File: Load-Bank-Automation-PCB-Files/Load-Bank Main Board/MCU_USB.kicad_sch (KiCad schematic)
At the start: 19 parts, among them J26 STM32-Prog-Header, SW2 SW_SPDT, SW4 RESET, U13 STM32G491VETx, U2 OXETDLJANF-8MHz

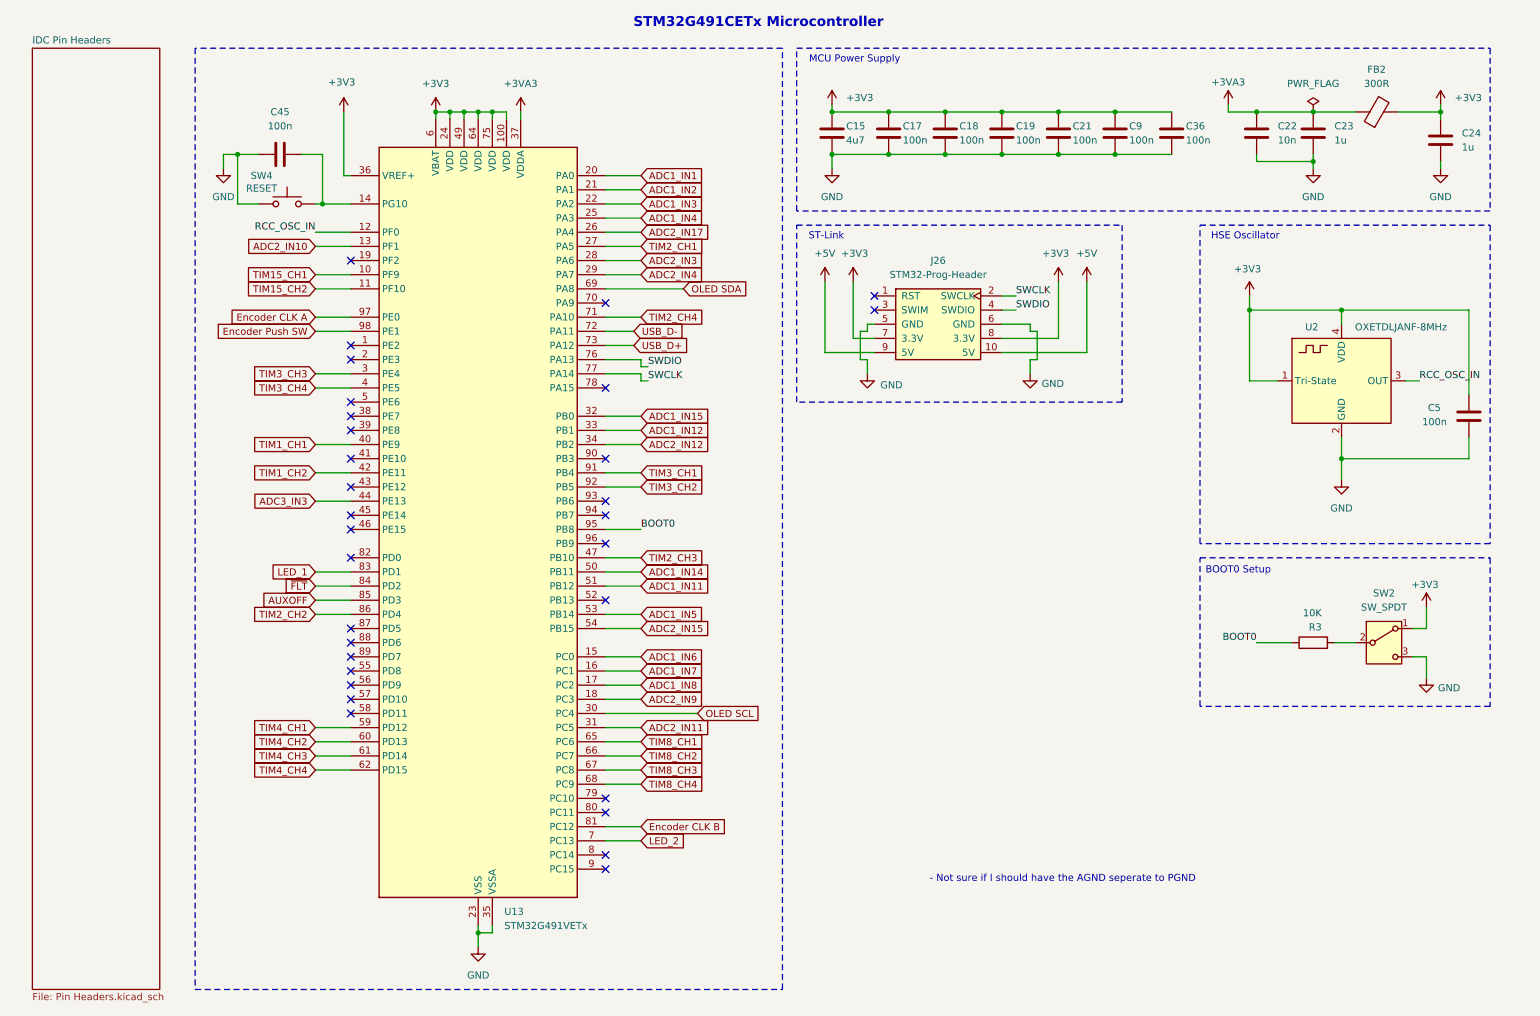
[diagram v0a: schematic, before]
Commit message: All footprints assigned and new schematic changes
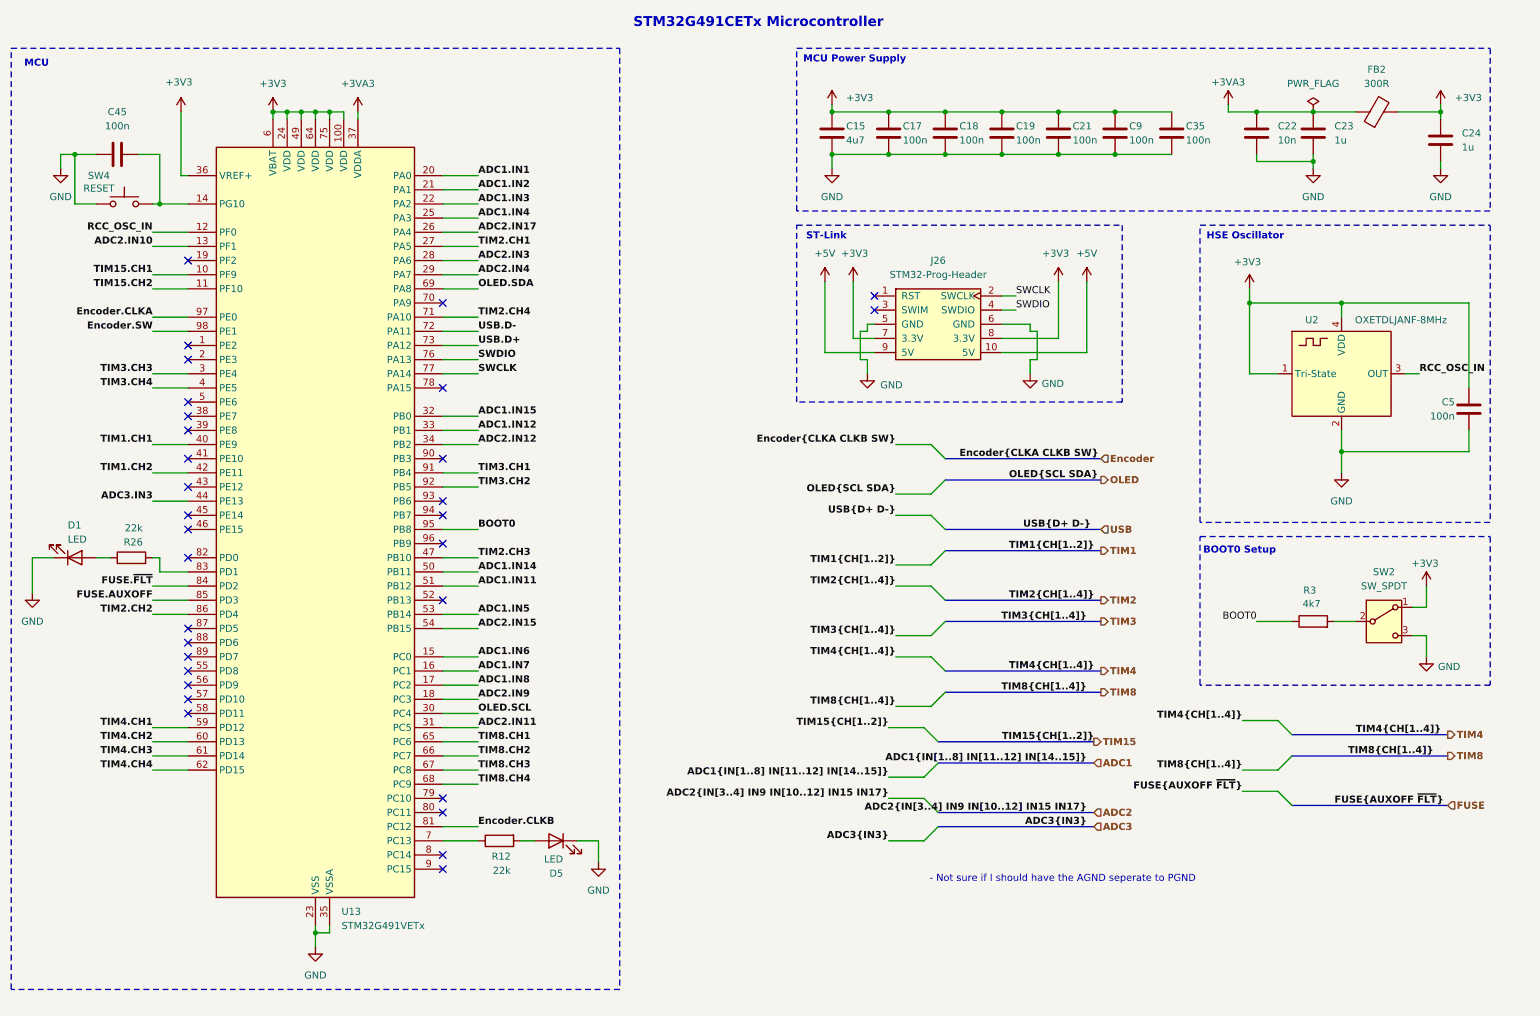
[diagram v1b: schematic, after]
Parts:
- removed C36: 100n, Capacitor_SMD:C_0603_1608Metric, symbol Device:C
- added C35: 100n, Capacitor_SMD:C_1206_3216Metric_Pad1.33x1.80mm_HandSolder, symbol Device:C
- added D1, D5: LED, LED_SMD:LED_0603_1608Metric, symbol Device:LED
- added R12, R26: 22k, Resistor_SMD:R_1206_3216Metric_Pad1.30x1.75mm_HandSolder, symbol Device:R
- C15: footprint Capacitor_SMD:C_0603_1608Metric -> Capacitor_SMD:C_0805_2012Metric_Pad1.18x1.45mm_HandSolder
- C17, C18, C19, C21, C45, C5, C9: footprint Capacitor_SMD:C_0603_1608Metric -> Capacitor_SMD:C_1206_3216Metric_Pad1.33x1.80mm_HandSolder
- C22, C23, C24: footprint Capacitor_SMD:C_0603_1608Metric -> Capacitor_SMD:C_0402_1005Metric_Pad0.74x0.62mm_HandSolder
- FB2: footprint Resistor_SMD:R_0603_1608Metric -> Resistor_SMD:R_0603_1608Metric_Pad0.98x0.95mm_HandSolder
- R3: value 10K -> 4k7; footprint Resistor_SMD:R_0603_1608Metric -> Resistor_SMD:R_1206_3216Metric_Pad1.30x1.75mm_HandSolder
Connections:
- net +3V3: now also C35.1
- net GND: now also C35.2, D1.1 (K), D5.1 (K)
- net ADC1_IN1 renamed ADC1.IN1
- net ADC1_IN11 renamed ADC1.IN11
- net ADC1_IN12 renamed ADC1.IN12
- net ADC1_IN14 renamed ADC1.IN14
- net ADC1_IN15 renamed ADC1.IN15
- net ADC1_IN2 renamed ADC1.IN2
- net ADC1_IN3 renamed ADC1.IN3
- net ADC1_IN4 renamed ADC1.IN4
- net ADC1_IN5 renamed ADC1.IN5
- net ADC1_IN6 renamed ADC1.IN6
- net ADC1_IN7 renamed ADC1.IN7
- net ADC1_IN8 renamed ADC1.IN8
- net ADC2_IN10 renamed ADC2.IN10
- net ADC2_IN11 renamed ADC2.IN11
- net ADC2_IN12 renamed ADC2.IN12
- net ADC2_IN15 renamed ADC2.IN15
- net ADC2_IN17 renamed ADC2.IN17
- net ADC2_IN3 renamed ADC2.IN3
- net ADC2_IN4 renamed ADC2.IN4
- net ADC2_IN9 renamed ADC2.IN9
- net ADC3_IN3 renamed ADC3.IN3
- net AUXOFF renamed FUSE.AUXOFF
- net Encoder CLK A renamed Encoder.CLKA
- net Encoder CLK B renamed Encoder.CLKB
- net Encoder Push SW renamed Encoder.SW
- net LED_1: no longer names the net of U13.83 (PD1)
- net LED_1: now also R26.2
- net LED_2: no longer names the net of U13.7 (PC13)
- net LED_2: now also R12.1
- net OLED SCL renamed OLED.SCL
- net OLED SDA renamed OLED.SDA
- net TIM15_CH1 renamed TIM15.CH1
- net TIM15_CH2 renamed TIM15.CH2
- net TIM1_CH1 renamed TIM1.CH1
- net TIM1_CH2 renamed TIM1.CH2
- net TIM2_CH1 renamed TIM2.CH1
- net TIM2_CH2 renamed TIM2.CH2
- net TIM2_CH3 renamed TIM2.CH3
- net TIM2_CH4 renamed TIM2.CH4
- net TIM3_CH1 renamed TIM3.CH1
- net TIM3_CH2 renamed TIM3.CH2
- net TIM3_CH3 renamed TIM3.CH3
- net TIM3_CH4 renamed TIM3.CH4
- net TIM4_CH1 renamed TIM4.CH1
- net TIM4_CH2 renamed TIM4.CH2
- net TIM4_CH3 renamed TIM4.CH3
- net TIM4_CH4 renamed TIM4.CH4
- net TIM8_CH1 renamed TIM8.CH1
- net TIM8_CH2 renamed TIM8.CH2
- net TIM8_CH3 renamed TIM8.CH3
- net TIM8_CH4 renamed TIM8.CH4
- net USB_D+ renamed USB.D+
- net USB_D- renamed USB.D-
- net ~{FLT} renamed FUSE.~{FLT}
- new net: D1.2 (A), R26.1
- new net: D5.2 (A), R12.2
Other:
- removed sheet IDC Pin Headers
- note added: "MCU"
- moved on the sheet: C45, SW2, SW4, U13, U2

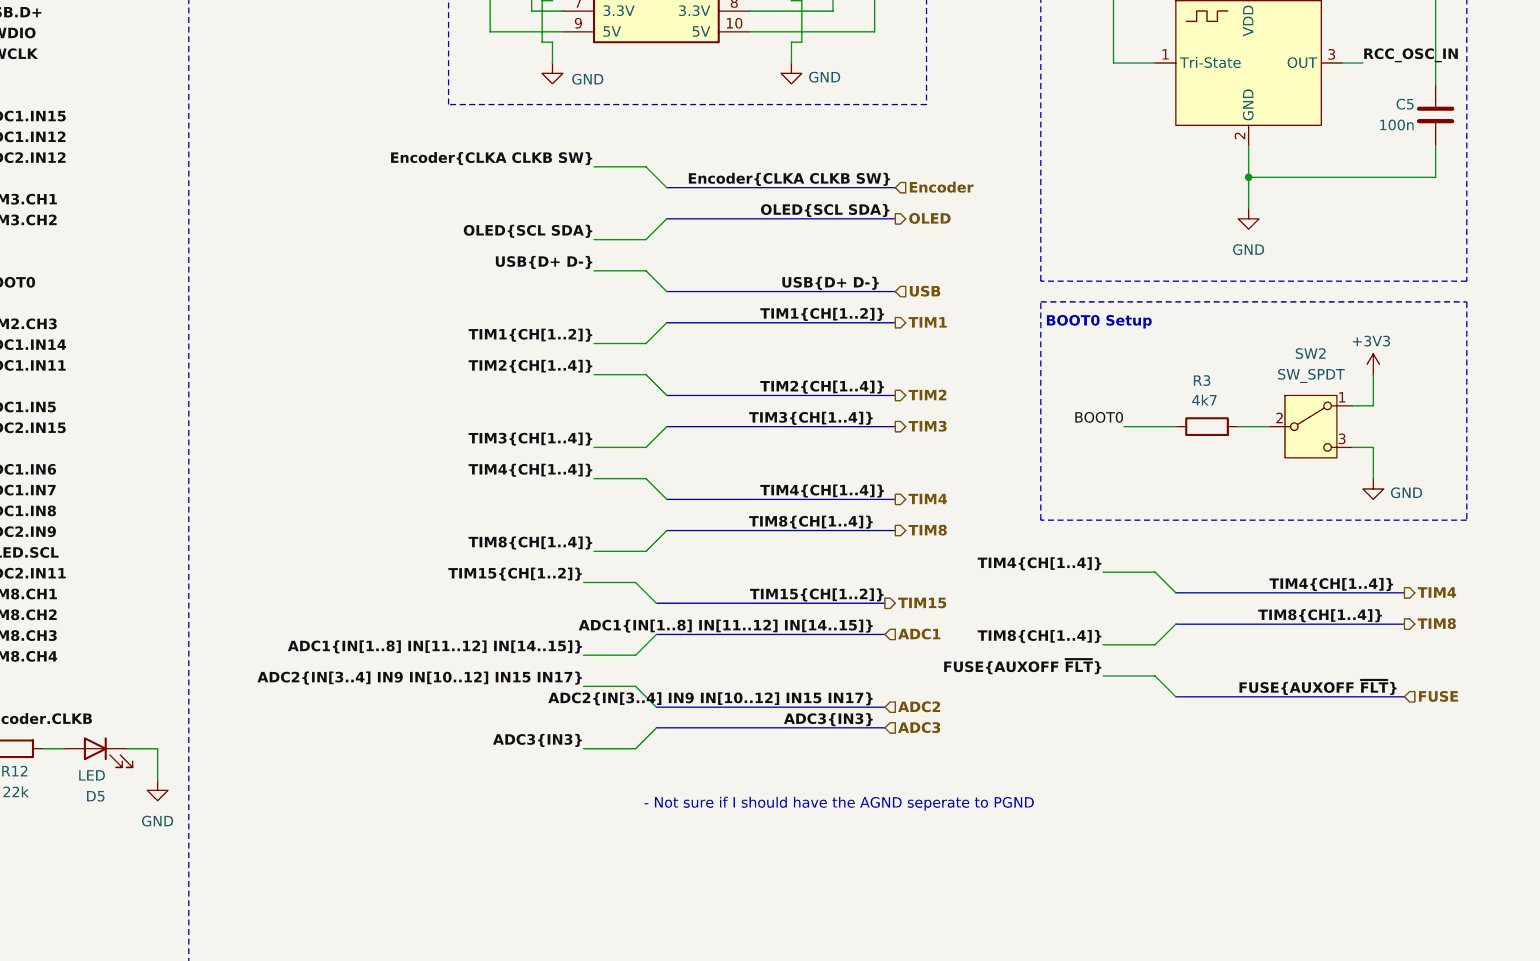
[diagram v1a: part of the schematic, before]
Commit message: Schematic complete and  ready for review
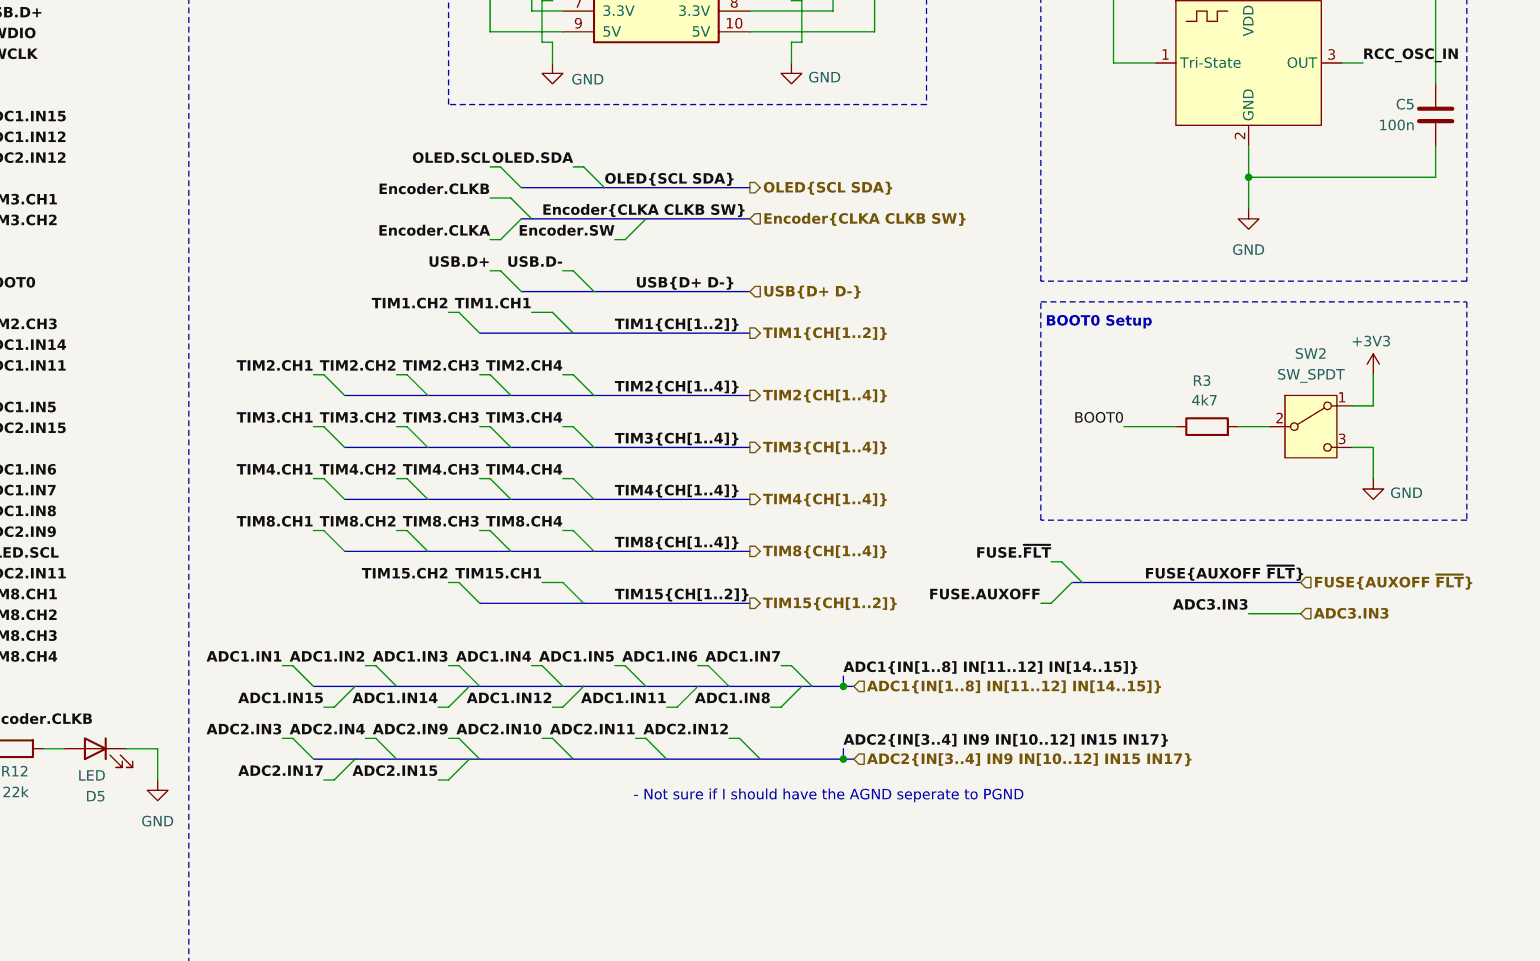
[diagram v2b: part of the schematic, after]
